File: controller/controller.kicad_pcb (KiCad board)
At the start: 2 copper layers, 139.7 x 100.3 mm, 28 parts, among them J1 PC104_40Pin_2.54mm, J2 Siren, U1 FM24W256-G, U2 SC16IS752IPW, U3 ADT7410TRZ, U4 MAX732MJA883B, X1 1.8432 MHz

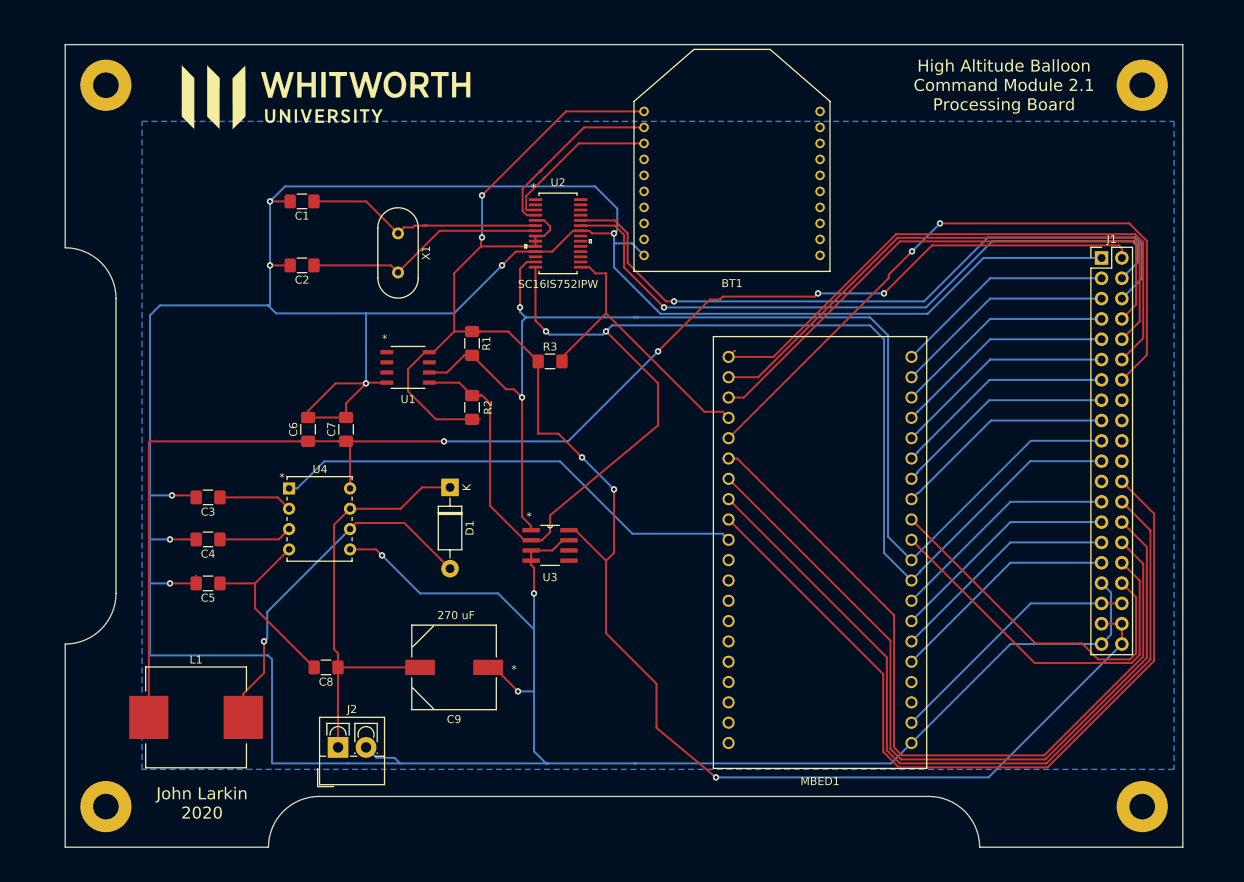
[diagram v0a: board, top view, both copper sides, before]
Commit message: First commit: Proteus III PCB footprint
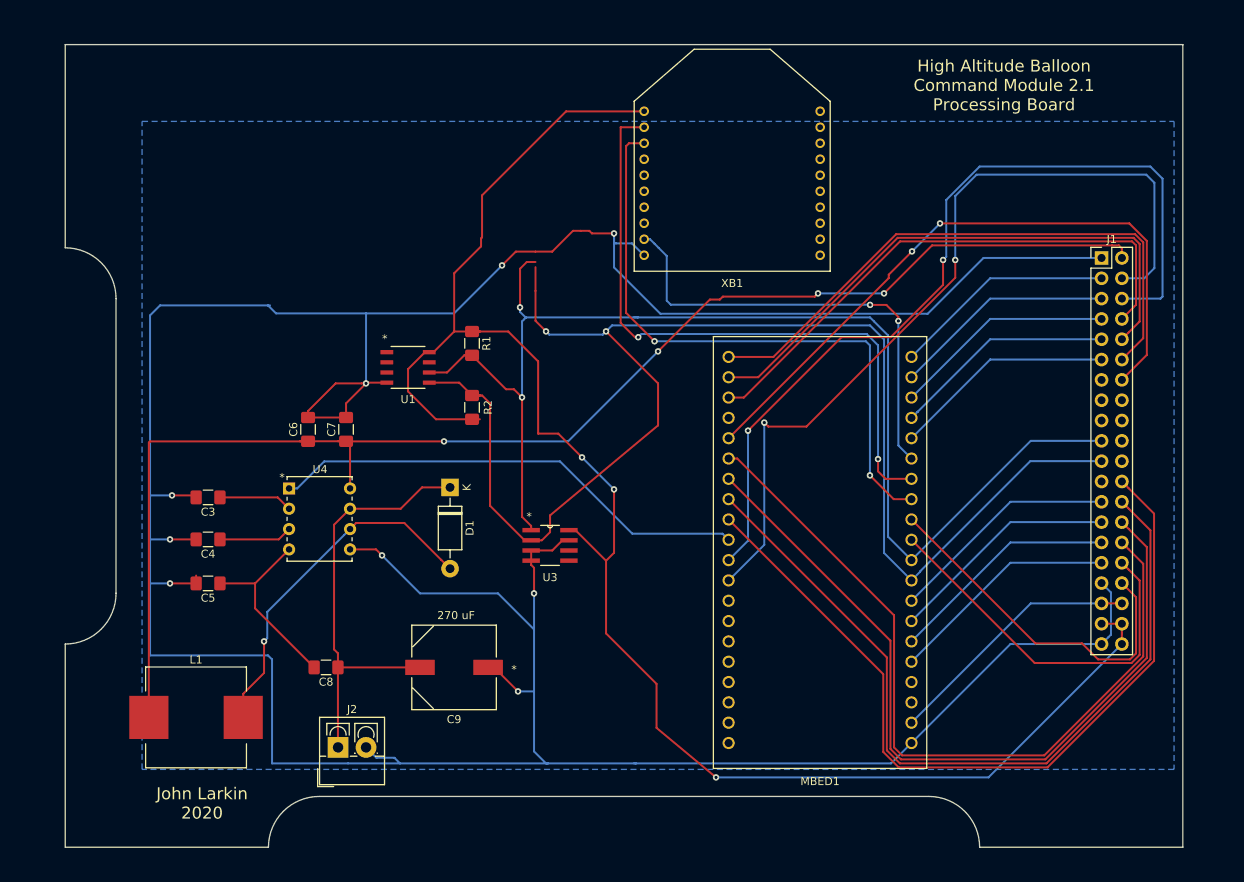
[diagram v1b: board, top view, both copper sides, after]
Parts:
- removed BT1: RN41, WhitworthStandard:xbee-standard
- removed C1: 22 pF, Capacitor_SMD:C_1206_3216Metric_Pad1.42x1.75mm_HandSolder
- removed C2: 33 pF, Capacitor_SMD:C_1206_3216Metric_Pad1.42x1.75mm_HandSolder
- removed G***: LOGO, WhitworthStandard:LOGO
- removed R3: 1k, Resistor_SMD:R_1206_3216Metric_Pad1.42x1.75mm_HandSolder
- removed REF** (x4): MountingHole_3.2mm_M3_Pad, MountingHole:MountingHole_3.2mm_M3_Pad
- removed U2: SC16IS752IPW, SC16IS752:SC16IS752IPW
- removed X1: 1.8432 MHz, Crystal:Crystal_HC49-U_Vertical
- added XB1: XBee, WhitworthStandard:xbee-standard, F.Cu at (108.8, 33.7)
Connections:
- J1 pad 24: /RADIO_WAKE -> Net-(J1-Pad24)
- J1 pad 38: /RADIO_RX -> /USB_D+
- J1 pad 39: /RADIO_TX -> /USB_D-
- J1 pad 7: /POD_WAKE -> Net-(J1-Pad7)
- J1 pad 8: /POD_TX -> Net-(J1-Pad8)
- J1 pad 9: /POD_RX -> Net-(J1-Pad9)
- MBED1 pad 13: /POD_RX -> /Local_RX
- MBED1 pad 14: /POD_TX -> /Local_TX
- MBED1 pad 15: /POD_WAKE -> /Local_WAKE
- MBED1 pad 24: /SERIAL_ALERT -> Net-(MBED1-Pad24)
- MBED1 pad 31: Net-(MBED1-Pad31) -> /USB_D+
- MBED1 pad 32: Net-(MBED1-Pad32) -> /USB_D-
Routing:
- net /USB_D+: track 0.00 -> 109.2 mm, vias 0 -> 2
- net /USB_D-: track 0.00 -> 105.3 mm, vias 0 -> 2
- net /RADIO_RX: track 88.0 -> 0.00 mm, vias 1 -> 0
- net /RADIO_TX: track 84.9 -> 0.00 mm, vias 1 -> 0
- net /Local_TX: track 0.00 -> 81.4 mm, vias 0 -> 2
- net /Local_RX: track 0.00 -> 78.1 mm, vias 0 -> 2
- net GND: track 517.8 -> 451.2 mm, vias 11 -> 9
- net /Local_WAKE: track 0.00 -> 57.5 mm, vias 0 -> 2
- net /SERIAL_ALERT: track 37.5 -> 0.00 mm
- net Net-(C2-Pad1): track 30.2 -> 0.00 mm
- net Net-(C1-Pad1): track 30.2 -> 0.00 mm
- net /POD_TX: track 27.9 -> 0.00 mm
- net /POD_WAKE: track 27.9 -> 0.00 mm
- net /POD_RX: track 27.8 -> 0.00 mm
- net /BT_RX: track 23.3 -> 0.00 mm
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
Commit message: Updated controller board with proteus III and Zilog multiplexer
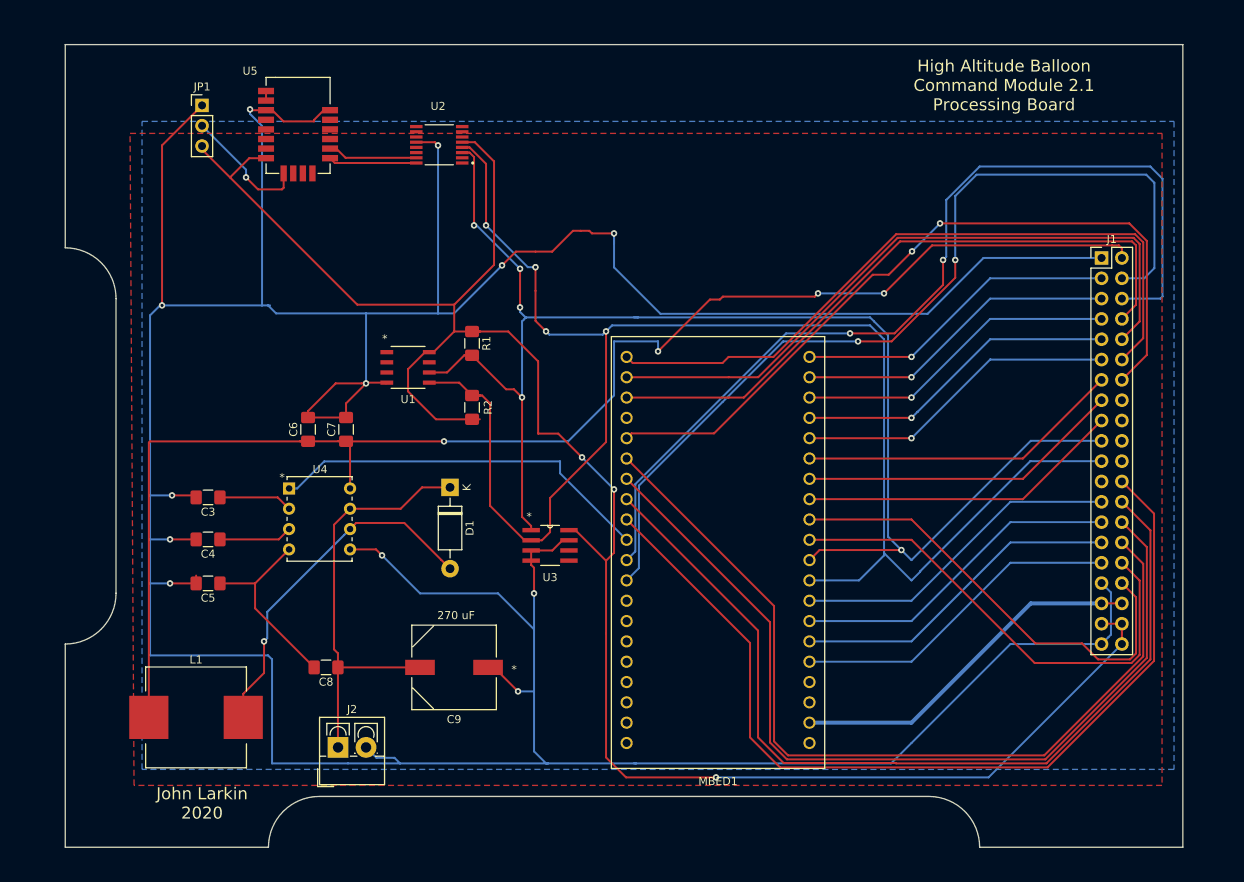
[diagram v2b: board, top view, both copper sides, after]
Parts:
- removed XB1: XBee, WhitworthStandard:xbee-standard
- added JP1: Jumper_3_Open, Connector_PinHeader_2.54mm:PinHeader_1x03_P2.54mm_Vertical, F.Cu at (42.5, 33.0)
- added U2: ZDU0110RFX, WhitworthStandard:ZDU0110RFX, F.Cu at (72.5, 38.0)
- added U5: ProteusIII, WhitworthStandard:Proteus_III_hand_solder, F.Cu at (54.5, 36.5)
- moved MBED1 12.8 mm to (107.0, 100.0)
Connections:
- J1 pad 24: Net-(J1-Pad24) -> /RADIO_WAKE
- J1 pad 7: Net-(J1-Pad7) -> /POD_WAKE
- J1 pad 8: Net-(J1-Pad8) -> /POD_TX
- J1 pad 9: Net-(J1-Pad9) -> /POD_RX
- MBED1 pad 13: /Local_RX -> /POD_RX
- MBED1 pad 14: /Local_TX -> /POD_TX
- MBED1 pad 15: /Local_WAKE -> /POD_WAKE
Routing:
- net GND: track 451.2 -> 534.2 mm, vias 9 -> 12
- net /Local_TX: track 81.4 -> 0.00 mm, vias 2 -> 0
- net /Local_RX: track 78.1 -> 0.00 mm, vias 2 -> 0
- net /Local_WAKE: track 57.5 -> 0.00 mm, vias 2 -> 0
- net /POD_TX: track 0.00 -> 40.6 mm
- net /POD_WAKE: track 0.00 -> 40.6 mm
- net /POD_RX: track 0.00 -> 40.6 mm
- net +3V3: track 209.9 -> 246.8 mm
- net /I2C_SCL: track 157.8 -> 185.8 mm, vias 2 -> 5
- net /I2C_SDA: track 179.3 -> 204.0 mm, vias 2 -> 4
- net Net-(JP1-Pad2): track 0.00 -> 15.9 mm, vias 0 -> 1
- net /IRIDIUM_PWR_CTRL: track 101.3 -> 115.3 mm
- net /IRIDIUM_RX: track 99.8 -> 113.5 mm
- net /IRIDIUM_TX: track 98.2 -> 111.9 mm
- net /LED_C: track 74.4 -> 87.7 mm
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- added copper zone on F.Cu, net +3V3

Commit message: 2nd commit mounting through holes added
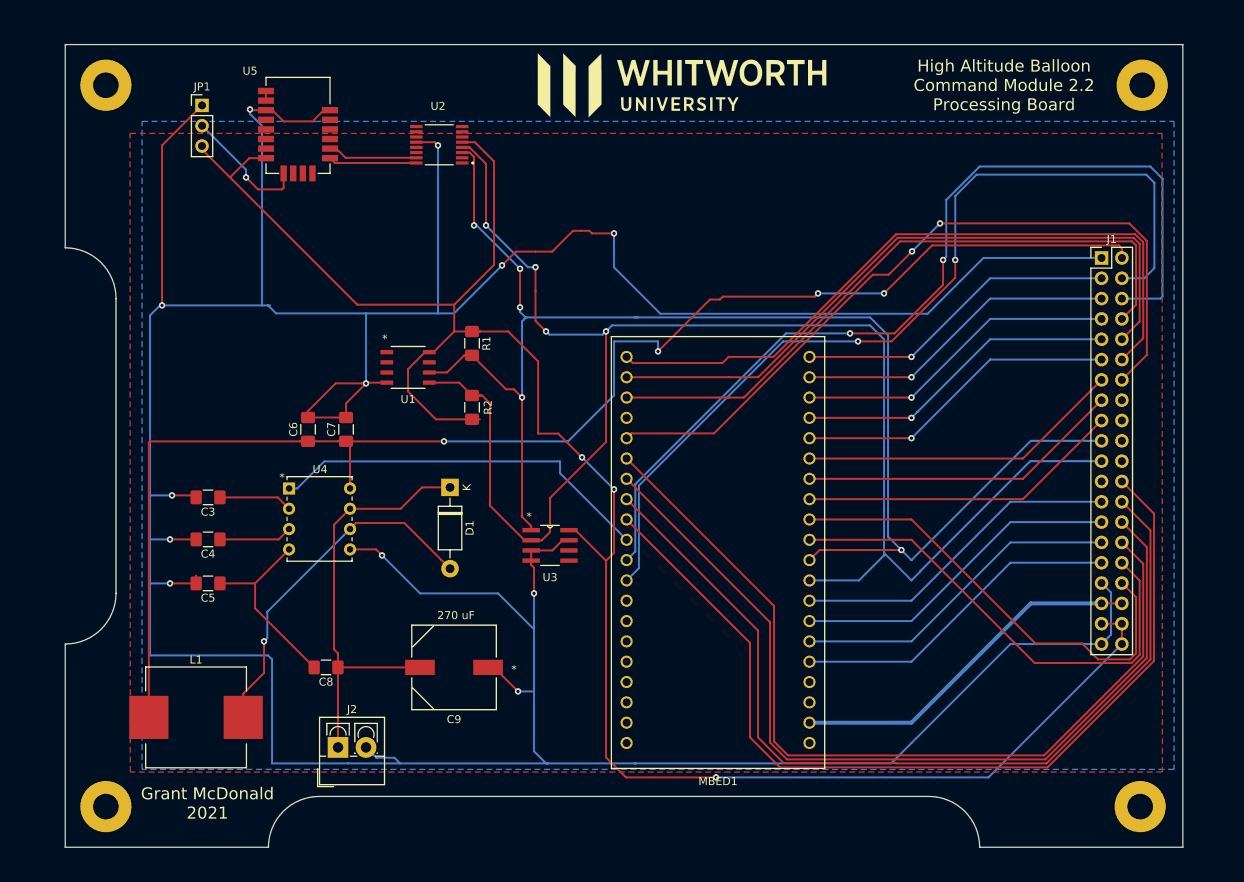
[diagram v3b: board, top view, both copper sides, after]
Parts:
- added G***: LOGO, WhitworthStandard:LOGO, F.Cu at (102.5, 30.5)
- added REF**: MountingHole_3.2mm_M3_Pad, MountingHole:MountingHole_3.2mm_M3_Pad, F.Cu at (160.0, 30.5)
- added REF**: MountingHole_3.2mm_M3_Pad, MountingHole:MountingHole_3.2mm_M3_Pad, F.Cu at (159.8, 120.7)
- added REF**: MountingHole_3.2mm_M3_Pad, MountingHole:MountingHole_3.2mm_M3_Pad, F.Cu at (30.5, 120.7)
- added REF**: MountingHole_3.2mm_M3_Pad, MountingHole:MountingHole_3.2mm_M3_Pad, F.Cu at (30.5, 30.5)
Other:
- board text added: "Grant McDonald 2021"
- board text added: "High Altitude Balloon Command Module 2.2 Processing Board"
- board text removed: "High Altitude Balloon Command Module 2.1 Processing Board"
- board text removed: "John Larkin 2020"

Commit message: ZDU0110RFX I2C address set
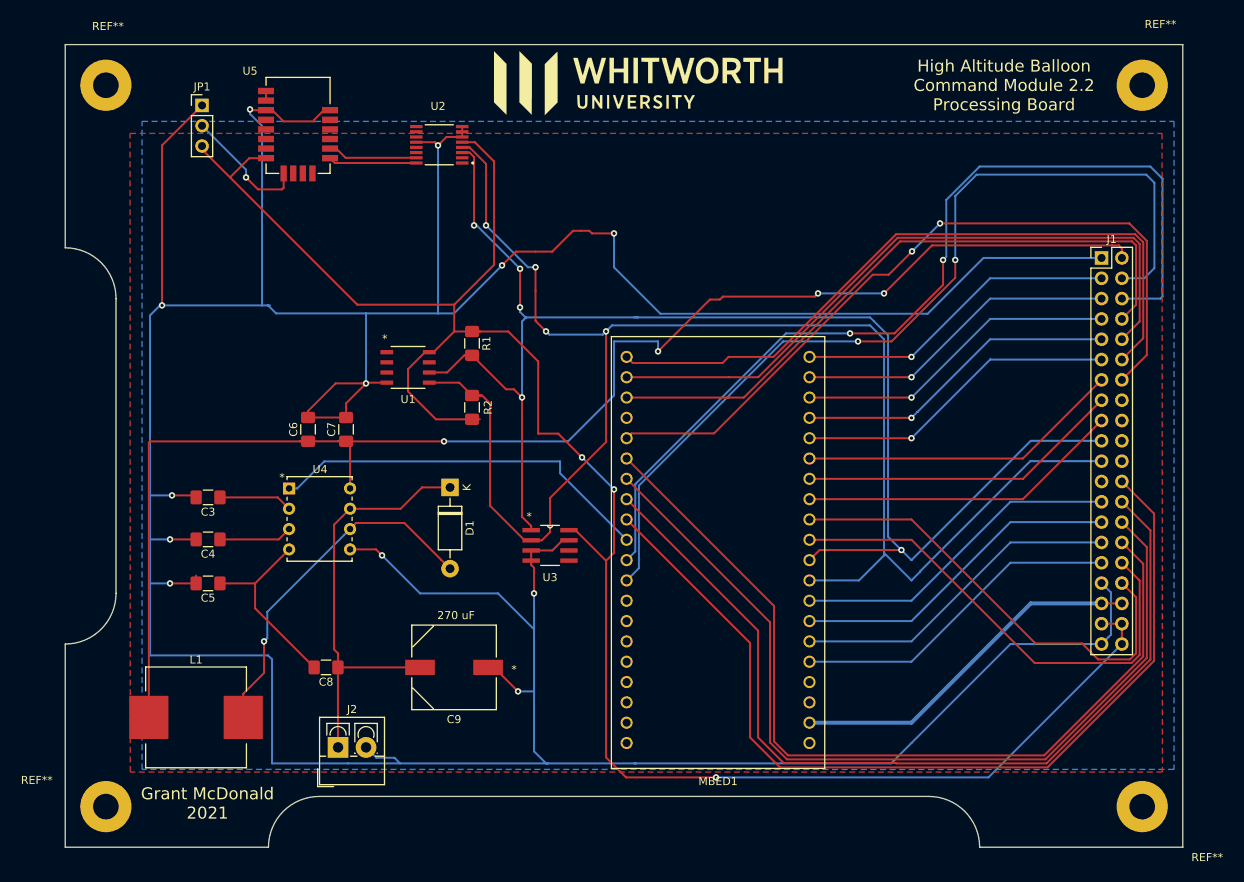
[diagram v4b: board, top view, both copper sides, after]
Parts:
- moved G*** 5.48 mm to (97.0, 30.2)
- moved REF** 0.25 mm to (160.0, 120.7)
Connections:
- U2 pad 6: Net-(U2-Pad6) -> GND
- U2 pad 7: Net-(U2-Pad7) -> GND
- U2 pad 8: Net-(U2-Pad8) -> GND
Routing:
- net GND: track 534.2 -> 539.0 mm

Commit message: Controller board 2.2
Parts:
- removed JP1: Jumper_3_Open, Connector_PinHeader_2.54mm:PinHeader_1x03_P2.54mm_Vertical
- added C1: 10uF, digikey-footprints:1206, F.Cu at (43.2, 63.8)
- added D2: 1N5817, Diode_THT:D_DO-41_SOD81_P10.16mm_Horizontal, F.Cu at (87.6, 109.2)
- D1: value D_Zener_ALT -> Zener 8.2 V
- U5: value ProteusIII -> RN4678-V_RM100; footprint WhitworthStandard:Proteus_III_hand_solder -> WhitworthStandard:RM100
- moved U5 12.4 mm to (46.7, 46.2)
- moved D1 0.76 mm to (73.7, 80.0)
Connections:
- J2 pad 1: Net-(C8-Pad1) -> Net-(D1-Pad2)
- L1 pad 2: Net-(D1-Pad2) -> Net-(D2-Pad2)
- MBED1 pad 24: Net-(MBED1-Pad24) -> /UART_INT
- U2 pad 6: GND -> /UART_INT
- U4 pad 6: Net-(D1-Pad2) -> Net-(D2-Pad2)
- U5 pad 1: Net-(U5-Pad1) -> GND
- U5 pad 13: /BT_TX -> Net-(U5-Pad13)
- U5 pad 14: /BT_RX -> Net-(U5-Pad14)
- U5 pad 18: GND -> Net-(U5-Pad18)
- U5 pad 2: Net-(U5-Pad1) -> GND
- U5 pad 4: Net-(U5-Pad4) -> +3V3
- U5 pad 8: +3V3 -> Net-(U5-Pad8)
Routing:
- net Net-(D2-Pad2): track 0.00 -> 61.1 mm, vias 0 -> 1
- net /UART_INT: track 0.00 -> 52.3 mm, vias 0 -> 1
- net GND: track 539.0 -> 519.8 mm, vias 12 -> 11
- net Net-(U5-Pad9): track 15.9 -> 0.00 mm, vias 1 -> 0
- net +3V3: track 246.8 -> 262.7 mm, vias 3 -> 5
- net Net-(D1-Pad2): track 44.3 -> 29.7 mm
- net /BT_RX: track 11.3 -> 24.0 mm
- net /BT_TX: track 11.0 -> 22.8 mm, vias 0 -> 2
- net Net-(C8-Pad1): track 54.7 -> 65.5 mm
- net Net-(U5-Pad1): track 1.20 -> 0.00 mm
- added copper zone on F.Cu, net GND
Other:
- board text added: "1N5817"
- board text added: "Zener 8.2 V"
